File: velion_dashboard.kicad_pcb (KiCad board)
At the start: 2 copper layers, 116 x 148 mm, 9 parts

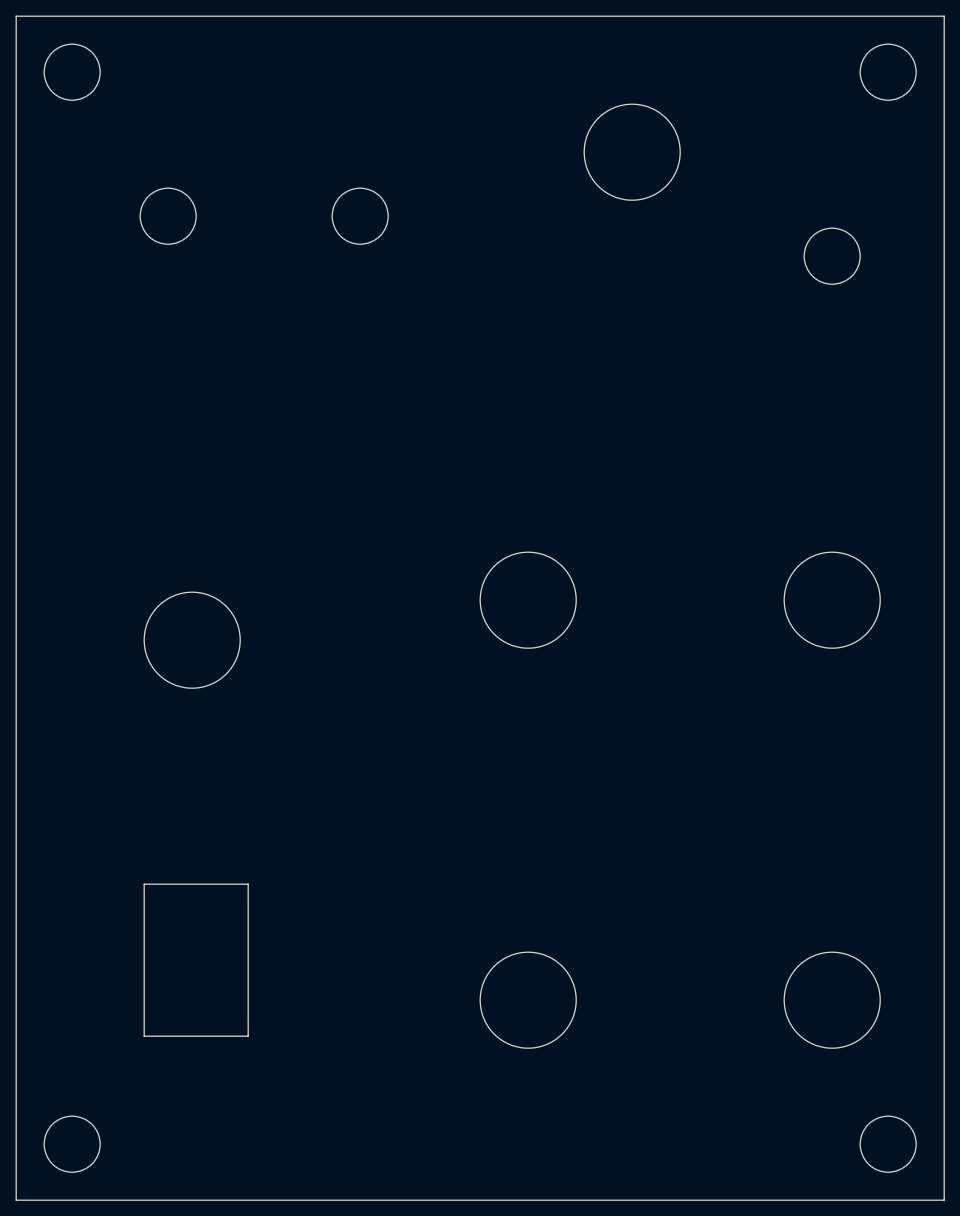
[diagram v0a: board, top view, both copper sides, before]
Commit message: added silkscreen with picto negative, added action to export pdf
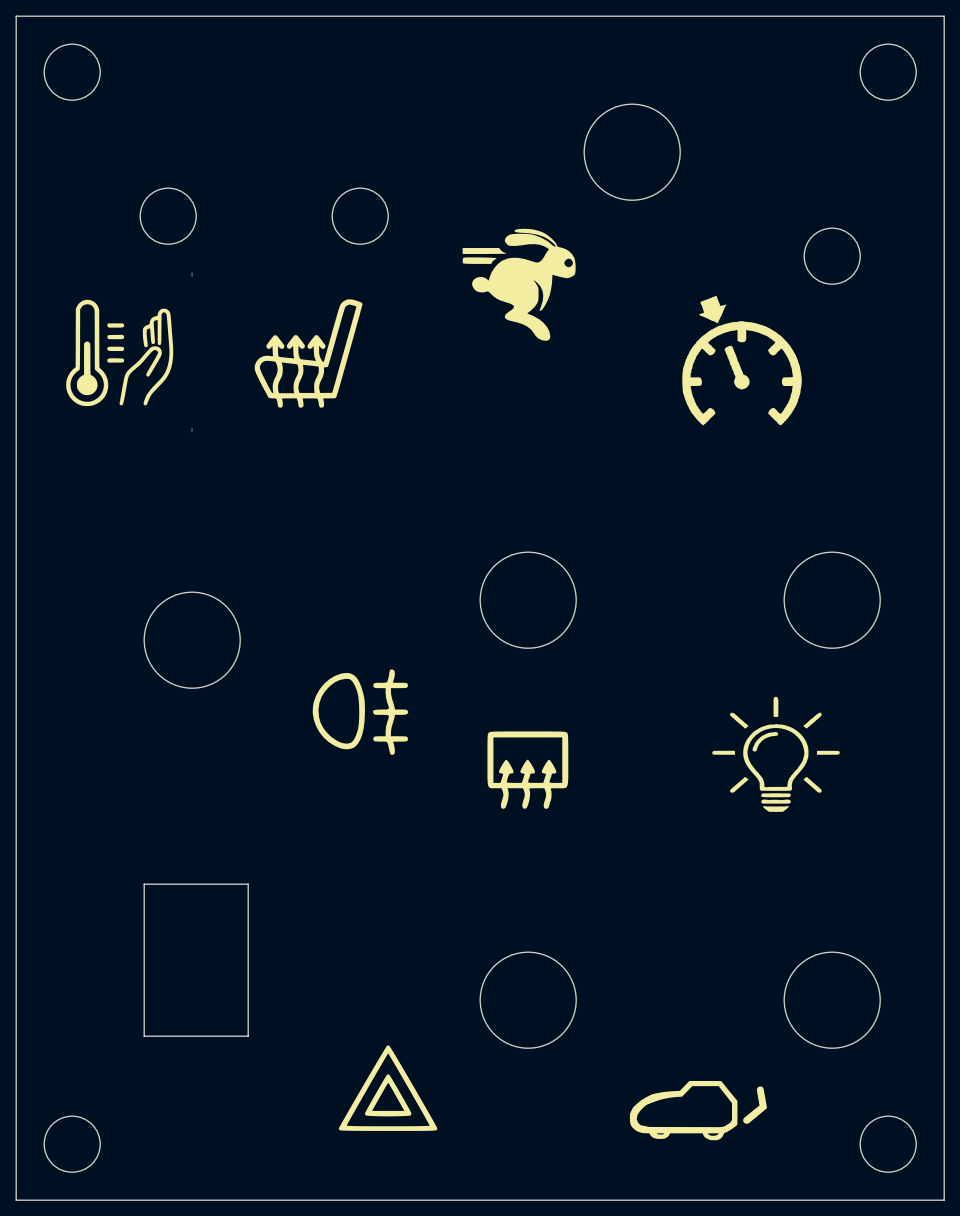
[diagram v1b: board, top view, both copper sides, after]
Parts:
- added G***: LOGO, picto:light_silk, F.Cu at (125.5, 122.0)
- added G***: LOGO, picto:seatwarmer_silk, F.Cu at (67.5, 72.0)
- added G***: LOGO, picto:defrost_silk, F.Cu at (95.0, 124.0)
- added G***: LOGO, picto:tempomat_silk, F.Cu at (121.0, 74.0)
- added G***: LOGO, picto:fog_silk, F.Cu at (74.0, 117.0)
- added G***: LOGO, picto:handwarmer_silk, F.Cu at (43.0, 72.0)
- added G***: LOGO, picto:mapping_silk, F.Cu at (94.5, 63.0)
- added G***: LOGO, picto:trunk_silk, F.Cu at (116.0, 165.5)
- added G***: LOGO, picto:warning_silk, F.Cu at (77.5, 165.0)
- moved G*** 4.50 mm to (67.5, 72.0)
- moved G*** 1.41 mm to (121.0, 74.0)
- moved G*** 1.00 mm to (116.0, 165.5)

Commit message: fixed hole size, added copper fill, remove ink stain
TODO : add copper negative for logo, check the fog light buttons + logo position
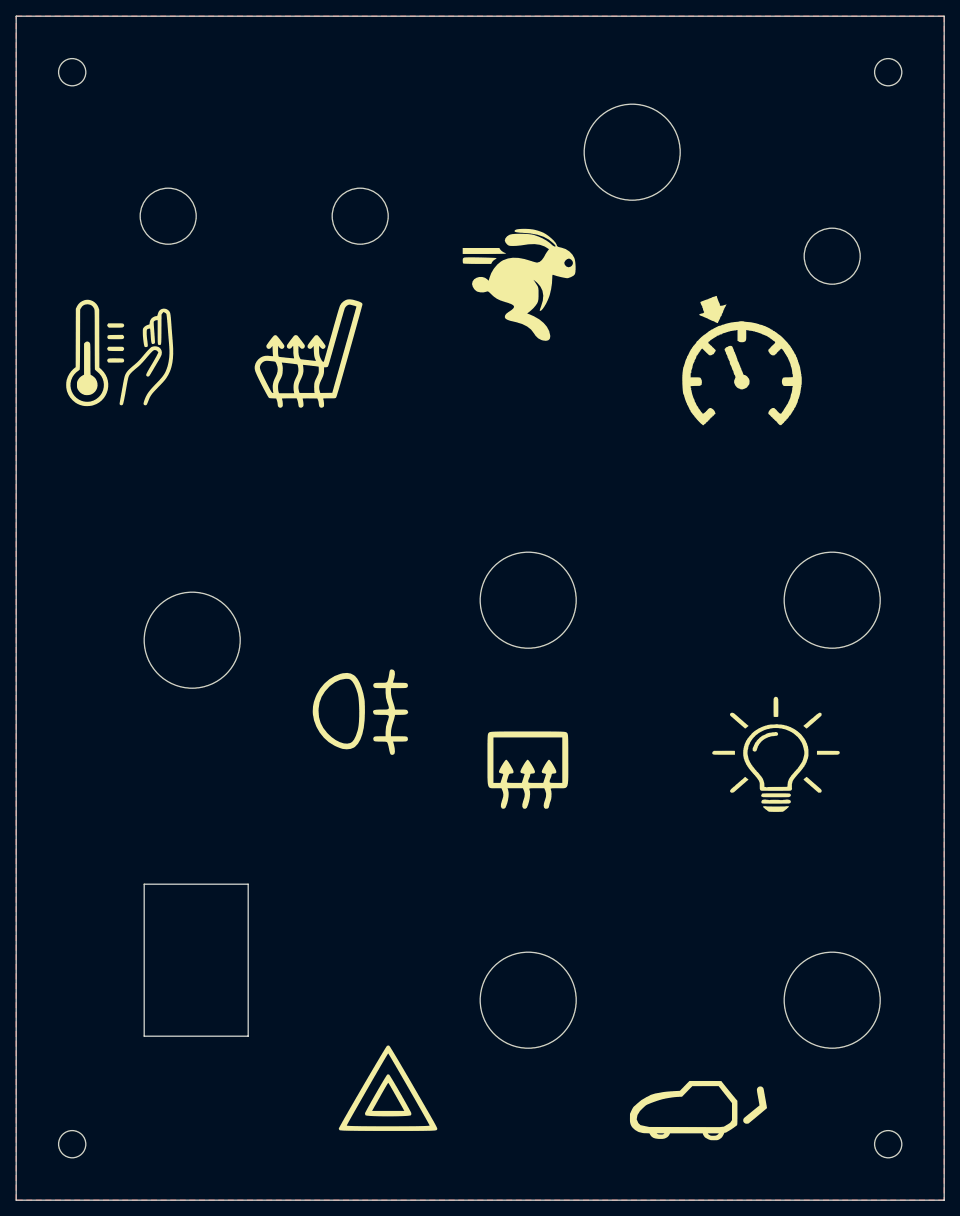
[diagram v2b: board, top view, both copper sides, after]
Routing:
- added copper zone on F.Cu, net (none)
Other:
- outline, holes or cut-outs redrawn
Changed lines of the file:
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@@
-		(fp_poly
-			(pts
-				(xy 9.993282 -9.996055) (xy 10.005613 -9.901773) (xy 10.011674 -9.759113) (xy 10.012073 -9.705399)
-				(xy 10.010655 -9.536743) (xy 10.005583 -9.433681) (xy 9.995633 -9.389688) (xy 9.979578 -9.39824)
-				(xy 9.961814 -9.437753) (xy 9.948116 -9.508138) (xy 9.94099 -9.61643) (xy 9.939952 -9.742381) (xy 9.944518 -9.865742)
-				(xy 9.954203 -9.966266) (xy 9.968522 -10.023705) (xy 9.975994 -10.030114)
-			)
-			(stroke
-				(width 0)
-				(type solid)
-			)
-			(fill yes)
-			(layer "F.SilkS")
-		)
-		(fp_poly
-			(pts
-				(xy 10.005285 9.482659) (xy 10.010871 9.617287) (xy 10.011521 9.696377) (xy 10.008093 9.85537) (xy 9.998024 9.968929)
-				(xy 9.982518 10.025734) (xy 9.975994 10.030113) (xy 9.957994 9.996423) (xy 9.945567 9.904714) (xy 9.940496 9.769027)
-				(xy 9.940467 9.750496) (xy 9.94506 9.609482) (xy 9.956694 9.492739) (xy 9.973016 9.422375) (xy 9.975994 9.416761)
-				(xy 9.99376 9.416604)
-			)
-			(stroke
-				(width 0)
-				(type solid)
-			)
-			(fill yes)
-			(layer "F.SilkS")
-		)
 		(fp_poly
 			(pts
@@
 	(gr_circle
 		(center 140 37)
-		(end 140 33.5)
+		(end 140 35.3)
 		(stroke
 			(width 0.05)
@@
 	(gr_circle
 		(center 38 37)
-		(end 38 33.5)
+		(end 38 35.3)
 		(stroke
 			(width 0.05)
@@
 	(gr_circle
 		(center 38 171)
-		(end 38 167.5)
+		(end 38 169.3)
 		(stroke
 			(width 0.05)
@@
 	(gr_circle
 		(center 140 171)
-		(end 140 167.5)
+		(end 140 169.3)
 		(stroke
 			(width 0.05)
@@
 		)
 	)
+	(zone
+		(net 0)
+		(net_name "")
+		(layer "F.Cu")
+		(hatch edge 0.5)
+		(connect_pads
+			(clearance 0.5)
+		)
+		(min_thickness 0.25)
+		(filled_areas_thickness no)
+		(fill yes
+			(thermal_gap 0.5)
+			(thermal_bridge_width 0.5)
+			(island_removal_mode 1)
+			(island_area_min 10)
+		)
+		(polygon
+			(pts
+				(xy 31 30) (xy 147 30) (xy 147 178) (xy 31 178)
+			)
+		)
+	)
